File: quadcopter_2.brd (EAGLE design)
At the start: 185.1 x 185.1 mm, 66 parts, among them J1 AVR_SPI_PRG_6NS, Q1 2.6A, Q2 2.6A, Q3 2.6A, Q4 2.6A, U1 ATMEGA128RFA1, U2 IMU_LSM9DS1TR, Y1 16MHz

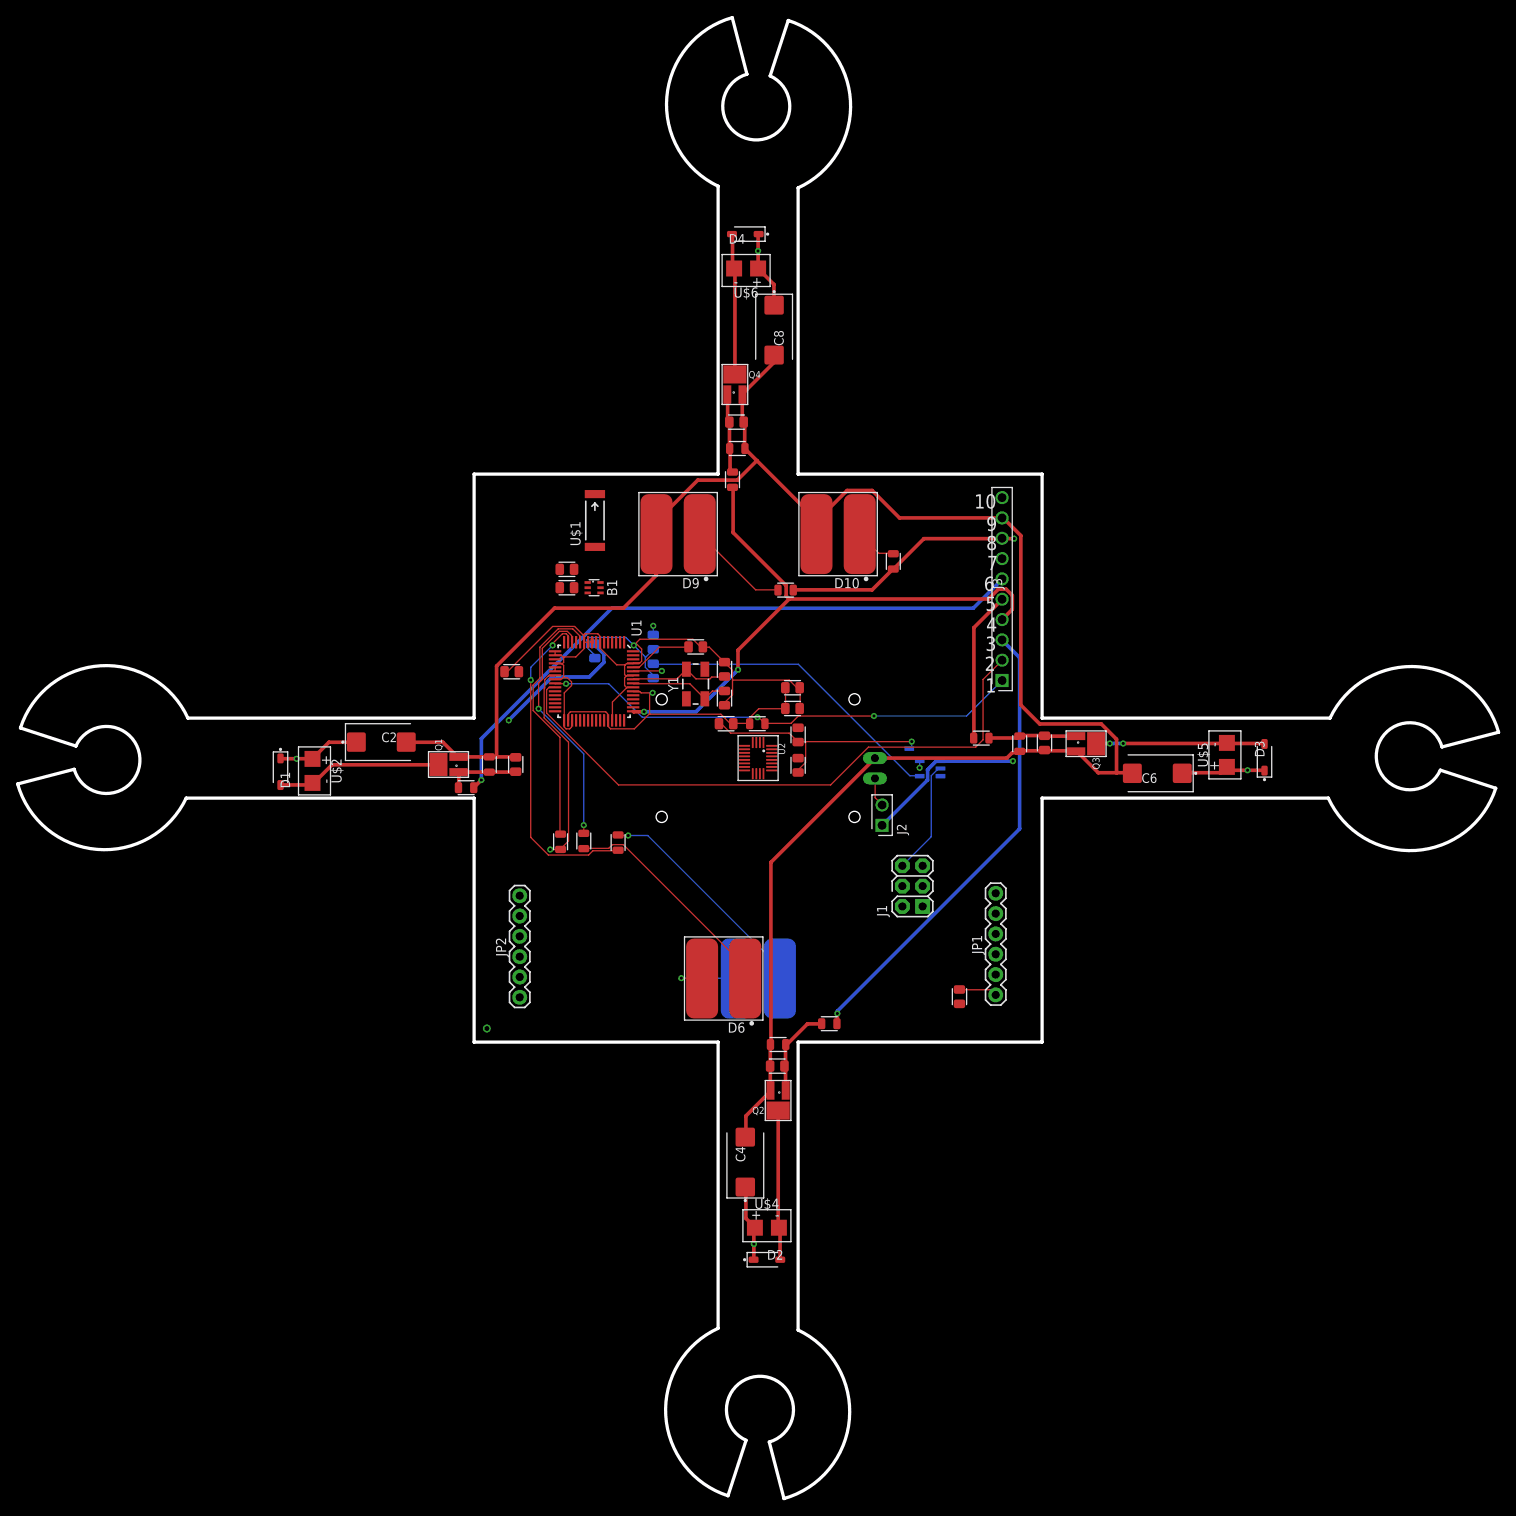
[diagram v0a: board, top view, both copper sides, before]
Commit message: fixed drc errors and routed 98%
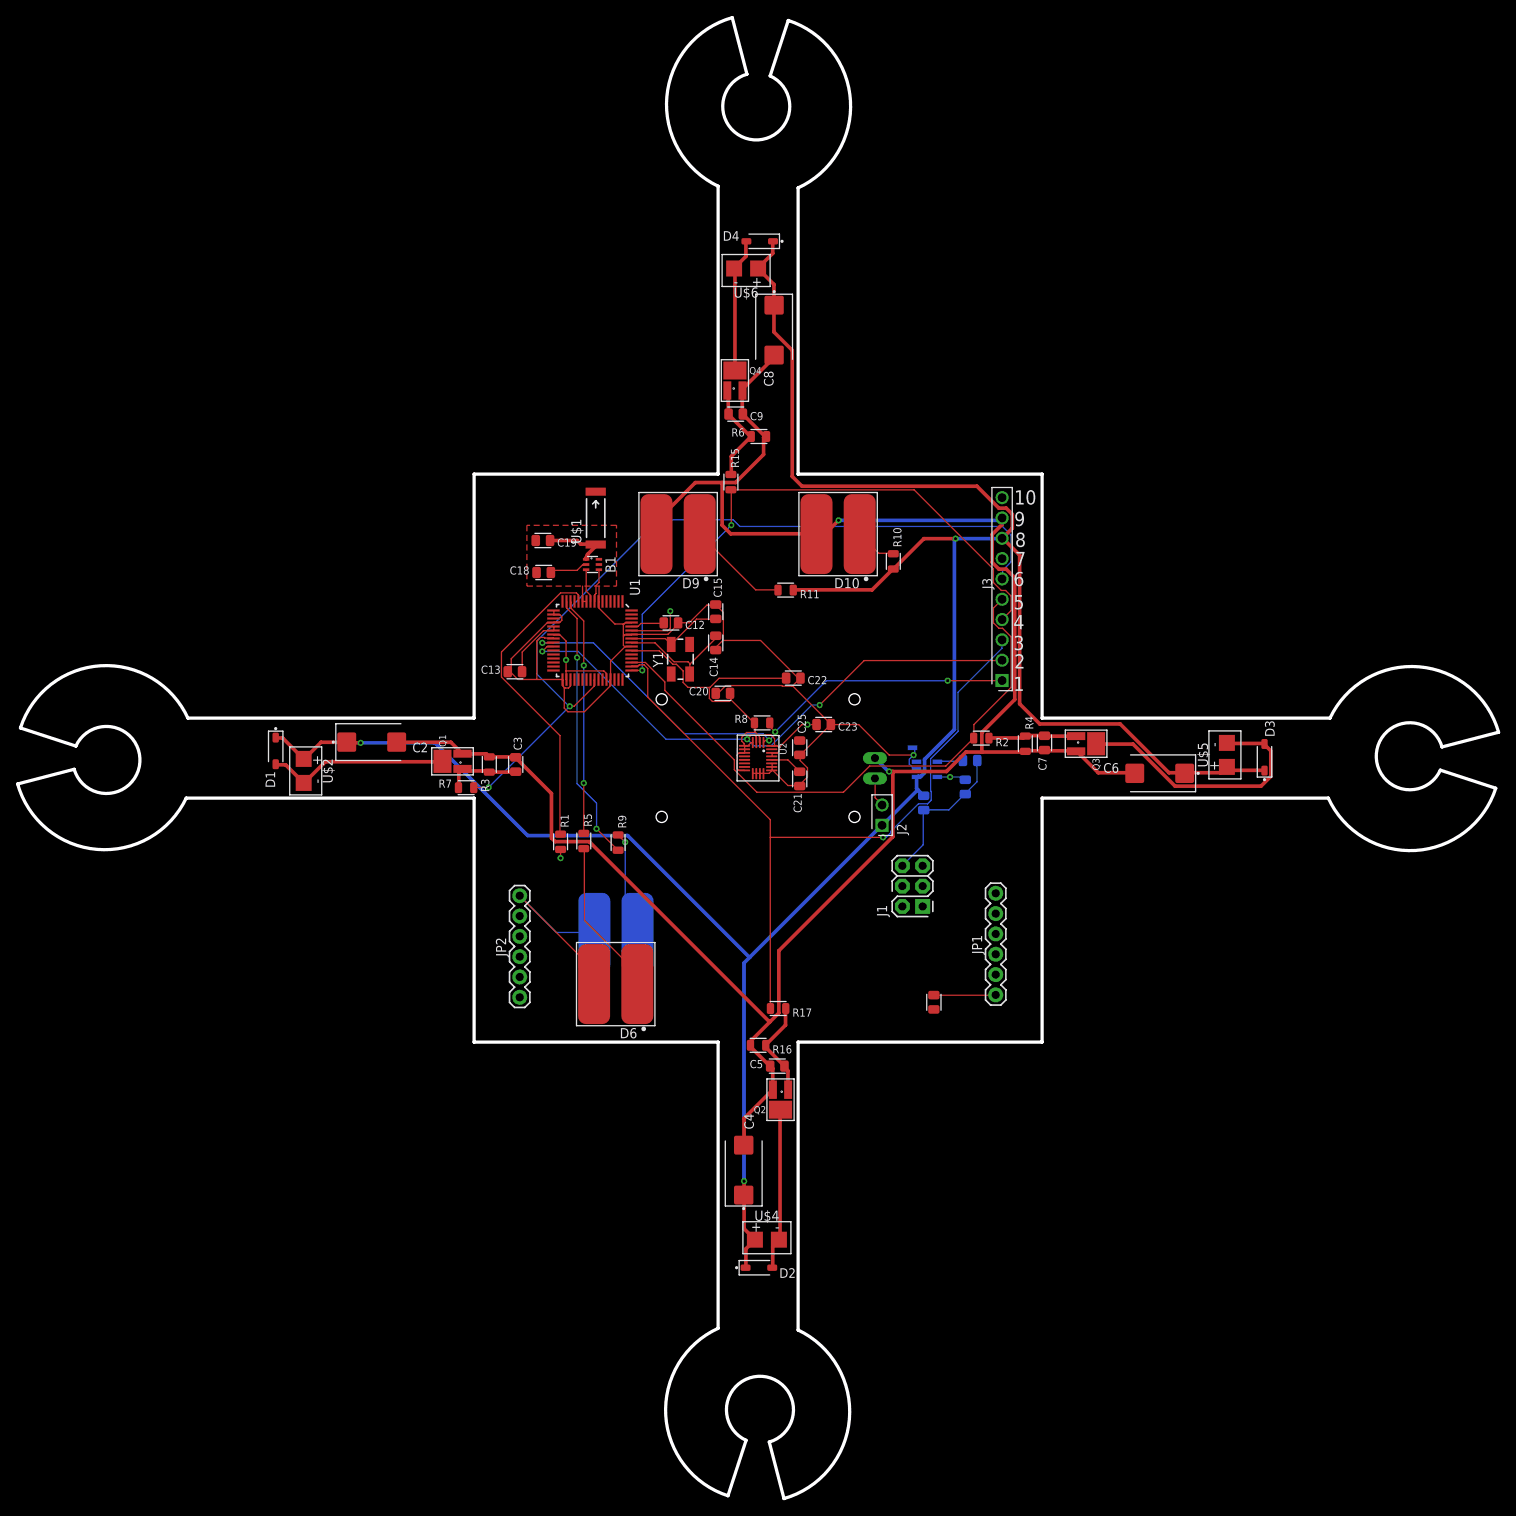
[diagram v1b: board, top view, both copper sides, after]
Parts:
- C14, C15: value 12pF -> 1uF
- C2, C4, C6, C8: value 100uF -> 220uF
- D1, D2, D3, D4: value 20V-500MA -> (none)
- moved C10 45.3 mm to (20.7, -5.60)
- moved C11 43.0 mm to (25.9, -3.60)
- moved C16 41.2 mm to (26.5, -0.30), turned to 180 degrees
- moved D5 18.7 mm to (-17.8, -21.9)
- moved D6 13.5 mm to (-17.8, -28.2)
- moved C15 7.28 mm to (-5.30, 18.3)
- moved C14 6.99 mm to (-5.30, 14.4)
- moved R17 6.68 mm to (2.50, -31.3), turned to 0 degrees
- moved U1 5.10 mm to (-20.7, 14.7)
- moved C19 4.69 mm to (-26.9, 27.2)
- moved C23 4.38 mm to (8.20, 4.20)
- moved C12 4.31 mm to (-10.9, 16.9)
- moved C20 3.82 mm to (-4.40, 8.10)
- moved Y1 3.64 mm to (-9.71, 12.4)
- moved C18 3.47 mm to (-26.8, 23.2)
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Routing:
- net VBAT: track 109.3 -> 327.0 mm, vias 8 -> 3
- net PE5: track 18.8 -> 74.6 mm
- net PE4: track 58.3 -> 97.1 mm
- net N$32: track 39.1 -> 3.31 mm
- net GND: track 156.6 -> 187.7 mm, vias 3 -> 1
- net PB5: track 79.9 -> 103.4 mm, vias 1 -> 2
- net N$19: track 28.5 -> 13.2 mm
- net N$24: track 21.1 -> 33.7 mm, vias 2 -> 0
- net SCL: track 60.2 -> 69.5 mm, vias 3 -> 4
- net 3V: track 71.6 -> 80.8 mm
- net N$28: track 28.2 -> 19.7 mm
- net RFANT: track 0.00 -> 8.25 mm
- net N$13: track 0.50 -> 8.03 mm
- net RESET: track 32.3 -> 39.5 mm
- net N$26: track 40.8 -> 33.8 mm
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- added copper zone on layer 1, net GND
- added copper zone on layer 2, net GND
- removed copper zone on layer 2, net N$35
- removed copper zone on layer 15, net N$36
